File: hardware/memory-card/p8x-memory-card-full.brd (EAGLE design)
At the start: 160 x 100 mm, 34 parts, among them J1 MABC96R, U1 28C256, U10 62256, U2 62256, U3 74HCT245, U4 74HCT30, U5 74HCT138, U6 74HCT138, U7 74HCT00, U8 74HCT32, U9 74HCT08

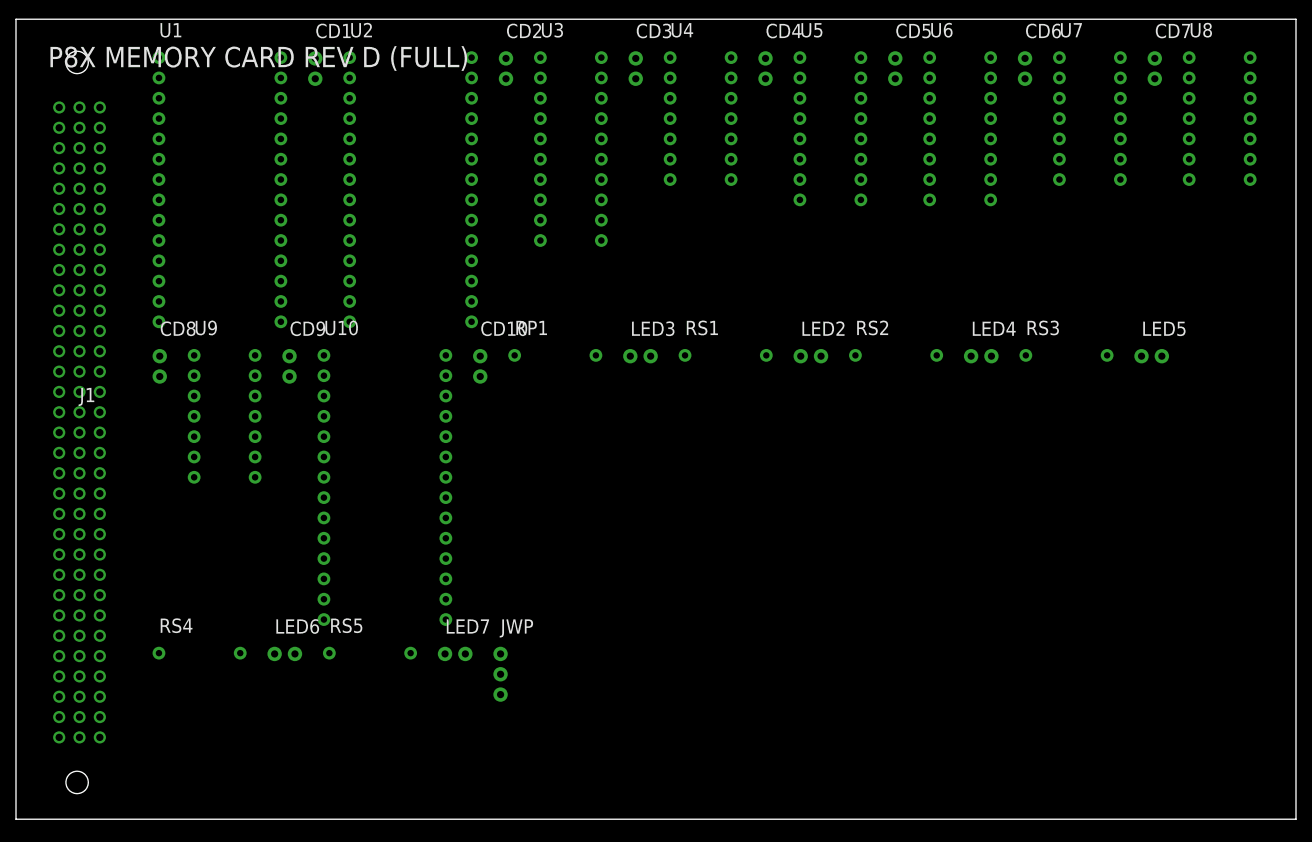
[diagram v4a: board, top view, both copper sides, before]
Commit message: feat: rev-E memory-card decode netlist (8K ROM, RAM from $2000)
Fold A13 into the memory-card address decode so the schematic netlist
matches the rev-E memory map (8K ROM $0000-$1FFF, RAM $2000-$FEFF) that
the emulator, firmware, OS, and docs already implement. Previously the
gen_eagle.py netlist still emitted the rev-D decode (ROM = OR(A14,A15),
a 16K window; A13 unrouted) under a "REV E" title.

Realized with exactly ONE added 2-input gate by reusing the rev-D gates
in place (rev D's spare gates were exhausted):
  Q      = OR(A13,A14)    -> U8.4  (was rev-D ROMCE = OR(A14,A15))
  ROM8CE = OR(Q, A15)     -> U11.1 (the one new gate; 74HCT32) = ROM !CE
                                    = A13|A14|A15 -> $0000-$1FFF (8K)
  -RAM2CE= NAND(!A15, Q)  -> U7.3  (was rev-D NAND(!A15,A14))
                                    = A15 OR NOR(A13,A14) -> $2000-$7FFF
U2 ($8000-$FEFF) unchanged. U11 is a 74HCT32 (only gate 1 used, spares
tied off); card() auto-adds its CD11 100nF decoupling cap and power pins.

gen_eagle validates errors=0 across all 8 boards; only the memory-card
artifacts changed. Regenerated the memory-card .sch/.brd/-full.brd and
the 3 PDFs (schematic, placement, full-placement). Updated the
memory-card README + theory-of-operation gate narration/diagram and
marked the BACKLOG item done.

Co-Authored-By: Claude Opus 4.8 <noreply@anthropic.com>
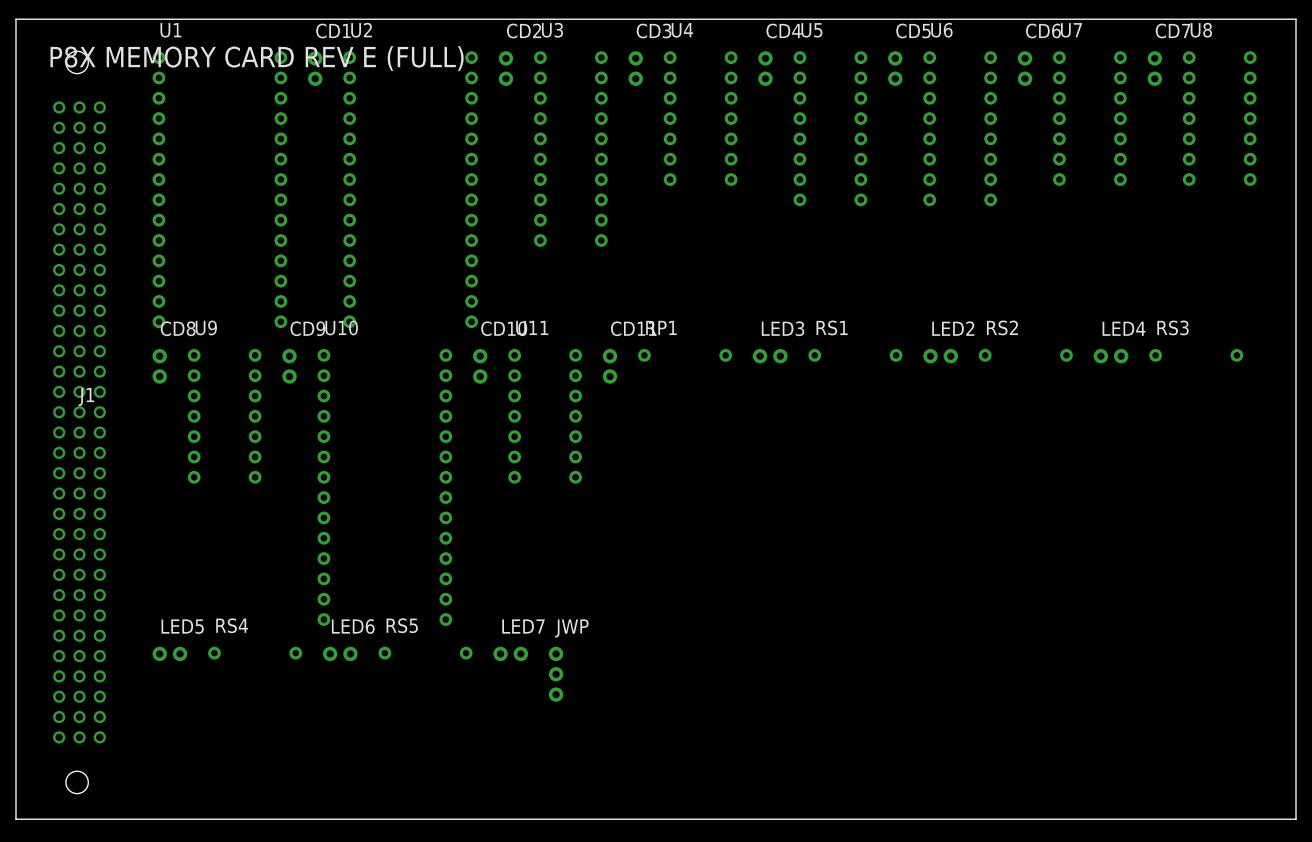
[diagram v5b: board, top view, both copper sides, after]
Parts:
- added CD11: 100N, p8x:C_DISC1
- added U11: 74HCT32, p8x:DIP14
- moved LED5 128.2 mm to (18.0, 20.7)
- moved LED4 16.2 mm to (135.6, 57.9)
- moved LED2 16.2 mm to (114.3, 57.9)
- moved LED3 16.2 mm to (93.0, 57.9)
- moved RP1 16.2 mm to (78.5, 58.0)
- moved RS1 16.2 mm to (99.8, 58.0)
- moved RS2 16.2 mm to (121.2, 58.0)
- moved RS3 16.2 mm to (142.4, 58.0)
- moved JWP 6.94 mm to (67.5, 20.7)
- moved LED6 6.94 mm to (39.3, 20.7)
- moved LED7 6.94 mm to (60.6, 20.7)
- moved RS4 6.94 mm to (24.8, 20.8)
- moved RS5 6.94 mm to (46.1, 20.8)
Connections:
- removed net ROMCE: U1.20, U8.11, U8.9
- new net Q: U11.1, U7.10, U8.11
- new net ROM8CE: U1.20, U11.3, U8.9
- net A13: now also U8.12
- net A14: no longer U7.10
- net A15: now also U11.2; no longer U8.12
- net GND: now also CD11.2, U11.10, U11.12, U11.13, U11.4, U11.5, U11.7, U11.9
- net VCC: now also CD11.1, U11.14
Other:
- board text added: "P8X MEMORY CARD REV E (FULL)"
- board text removed: "P8X MEMORY CARD REV D (FULL)"

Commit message: hardware: silkscreen off footprints, standard cap value format, backplane RL1->R1
Pre-Fusion cleanup so there is less to fix by hand once placing/routing.

1. SILKSCREEN NO LONGER OVERLAYS FOOTPRINTS (all boards). NAME/VALUE were emitted
   at the element origin +/-2.54 regardless of part size, so on anything bigger
   than a 2-pin part the text landed ON the pads -- the 96-pin DIN connector had
   J1/SLOT1 across its pad field, and caps had their values on top of them. Now
   placed against the real footprint bbox (fp_box): NAME 0.7mm above the top edge,
   VALUE 0.7mm below the bottom, left-aligned to the box. Verified: 1642
   silkscreen labels across all 9 boards, 0 sitting on a footprint (was many).
   Not rotation-aware, which is fine -- no board rotates a part today.

2. CAPACITOR VALUES use standard unit suffixes: 100N->100nF, 470U->470uF,
   150P->150pF, 1U->1uF (and the DNP/x10 variants). Applied everywhere, so the
   per-IC decoupling caps on every card change too. No doc quoted the raw value
   strings, so no doc churn.

3. BACKPLANE RL1 -> R1 (standard R designator). Scoped to the backplane section
   only -- the io-card and led-card have their own unrelated RL1 (8x330R networks)
   which are untouched. Backplane theory/design docs updated to match.

Part refs/values are decided in gen_eagle.py: the backplane `small=[...]` list and
each cards `ic`/`sm` dicts.

Co-Authored-By: Claude Opus 4.8 <noreply@anthropic.com>
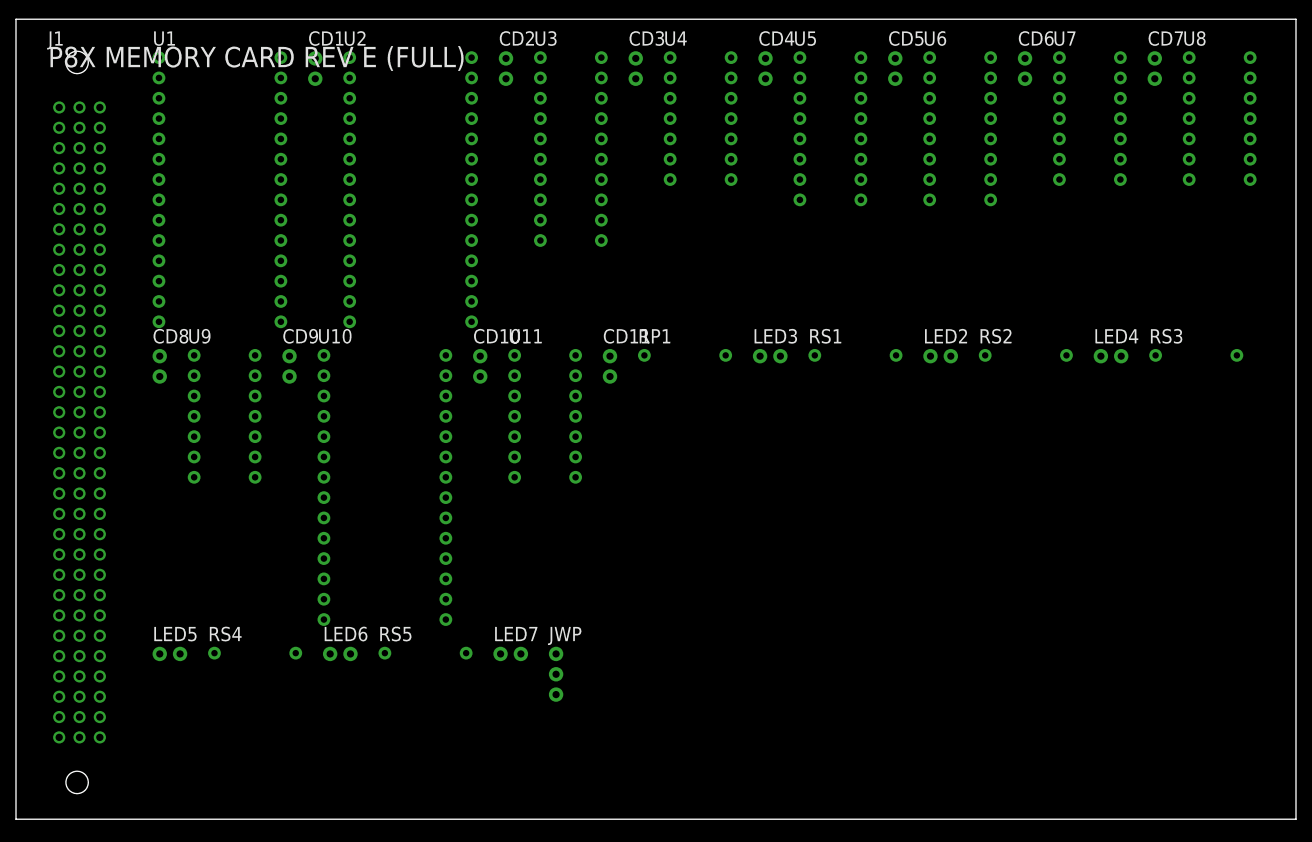
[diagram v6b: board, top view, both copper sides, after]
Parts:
- CD1, CD10, CD11, CD2, CD3, CD4, CD5, CD6, CD7, CD8, CD9: value 100N -> 100nF
